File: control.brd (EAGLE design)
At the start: 186 x 186 mm, 103 parts, among them CN1 40PIN FPC, CN2 MINI B USB, CN3 2X10 HEADER, CN4 2X10 HEADER, SW1 TACT, SW10 TACT, SW11 TACT, SW12 TACT, SW13 TACT, SW14 TACT, SW15 TACT, SW16 TACT, SW2 TACT, SW3 TACT, SW4 TACT, SW5 TACT, SW6 TACT, SW7 TACT, SW8 TACT, SW9 TACT, U1 STM32H743ZI, U2 AS4C8M16SA, U3 TPS61169, U4 USBLC6-2SC6, U5 FT230X, U6 DCDC 3V3

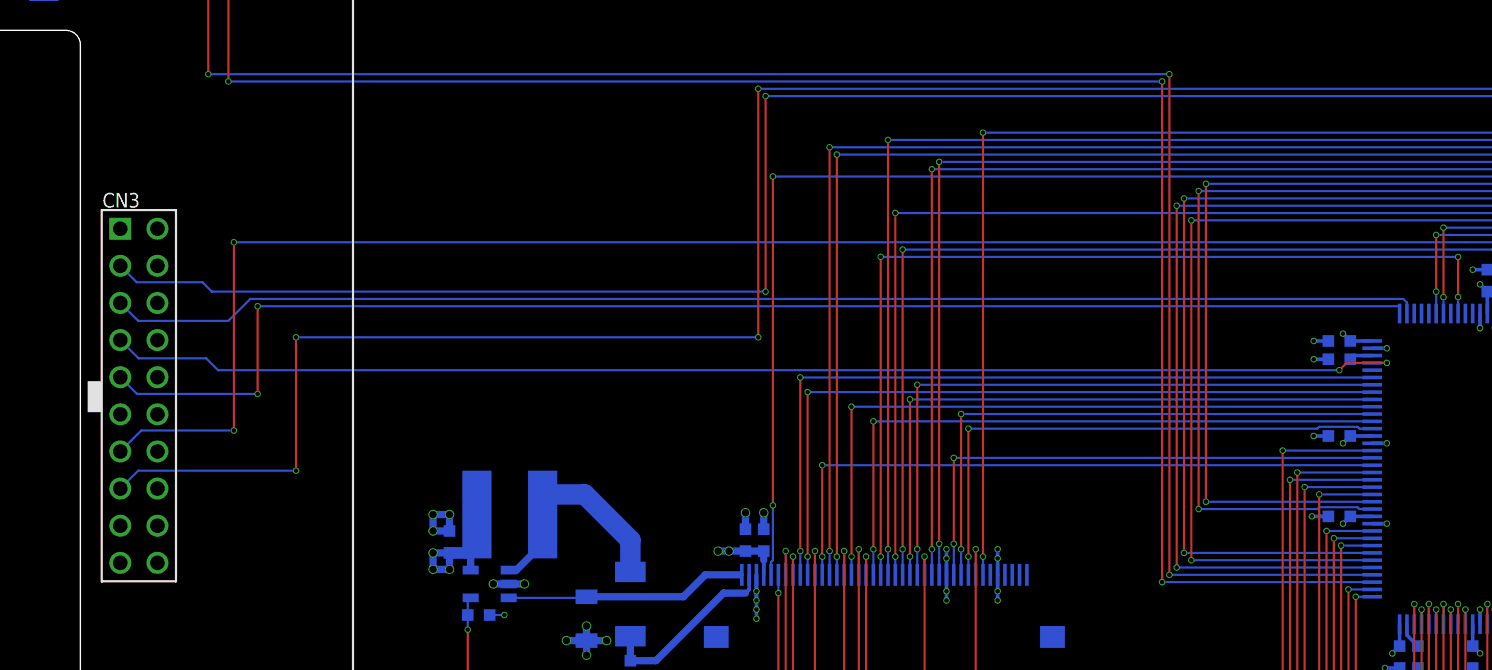
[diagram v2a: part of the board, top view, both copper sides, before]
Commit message: Corrected JTAG pinout
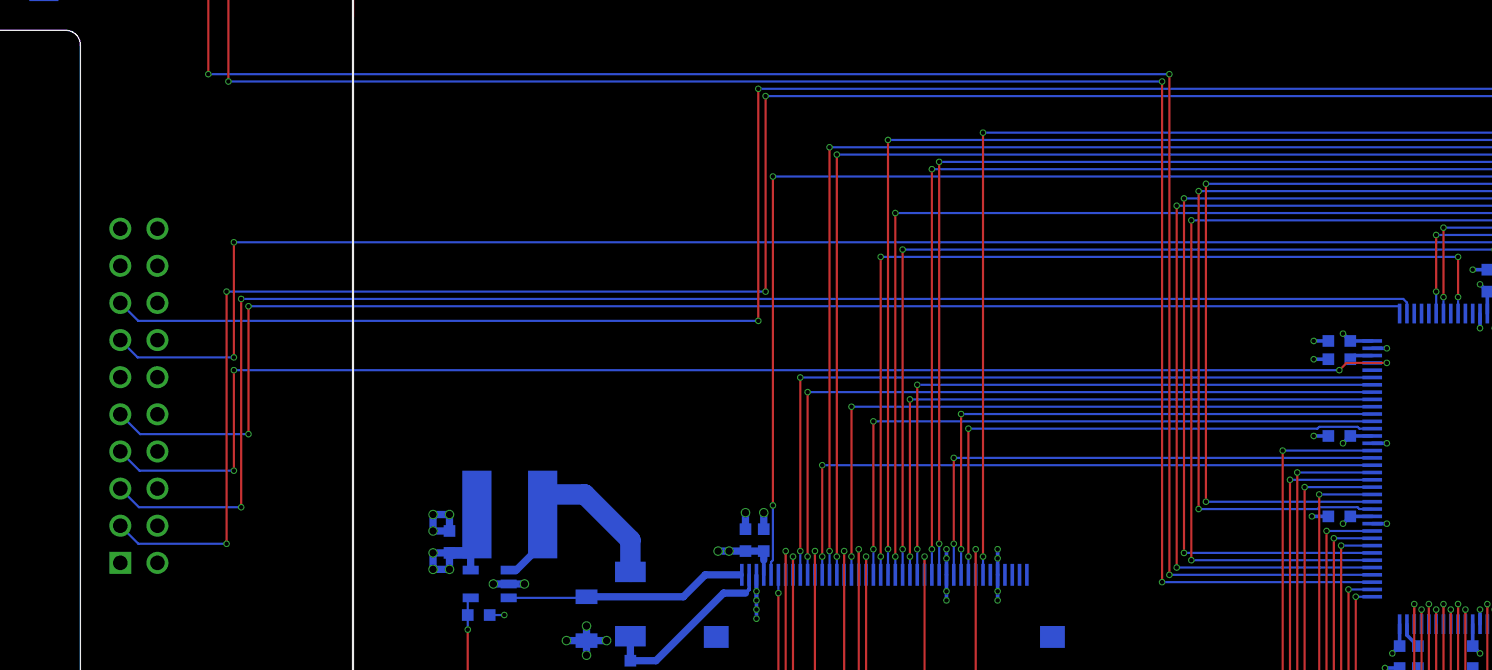
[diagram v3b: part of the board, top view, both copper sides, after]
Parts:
- flipped CN3 to the bottom, turned to 180 degrees
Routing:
- net JTAG_TRST: track 131.0 -> 148.0 mm, vias 4 -> 6
- net JTAG_TDI: track 90.0 -> 103.7 mm, vias 0 -> 2
- net STM_NRST: track 165.8 -> 155.5 mm, vias 6 -> 4
- net JTAG_TMS: track 88.7 -> 95.3 mm, vias 2 -> 4
- net JTAG_TDO: track 120.6 -> 115.5 mm
- net JTAG_TCK: track 94.5 -> 97.3 mm
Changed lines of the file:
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@@
 </layers>
 <board>
-<fusionsync huburn="a.cGVyc29uYWw6dWUyYjllNWFm" projecturn="a.cGVyc29uYWw6dWUyYjllNWFmIzIwMjAwODI1MzI2NDUzNDMx" f3durn="urn:adsk.wipprod:dm.lineage:wnPGf6KyQv68ik76HDulcw" pcbguid="" lastpulledtime="" lastsyncedchangeguid="" latestrevisionid="2ca1d1ef-4991-43c0-8b65-6e747995f1e9" lastsyncedrevisionid="2ca1d1ef-4991-43c0-8b65-6e747995f1e9" lastboardhashguid="514c7081-e8dd-fae7-9cc8-94f32975e53f" lastpushedtime="2020-10-09T13:18:08Z" linktopcb3d="true"/>
+<fusionsync huburn="a.cGVyc29uYWw6dWUyYjllNWFm" projecturn="a.cGVyc29uYWw6dWUyYjllNWFmIzIwMjAwODI1MzI2NDUzNDMx" f3durn="urn:adsk.wipprod:dm.lineage:wnPGf6KyQv68ik76HDulcw" pcbguid="" lastpulledtime="" lastsyncedchangeguid="" latestrevisionid="627856e7-1b0d-4a68-b278-4b2f0657c420" lastsyncedrevisionid="627856e7-1b0d-4a68-b278-4b2f0657c420" lastboardhashguid="c3fb2801-7401-a368-981a-5568be5e23b0" lastpushedtime="2020-10-11T09:29:11Z" linktopcb3d="true"/>
 <plain>
 <wire x1="90" y1="-93" x2="93" y2="-90" width="0" layer="20" curve="90" locked="yes"/>
@@
 <wire x1="60.35" y1="5" x2="55.35" y2="5" width="0.15" layer="29"/>
 <wire x1="60.35" y1="10" x2="60.35" y2="5" width="0.15" layer="29"/>
-<rectangle x1="-78.5" y1="48.875" x2="-77.5" y2="51" layer="21"/>
+<rectangle x1="-78.5" y1="48.875" x2="-77.5" y2="51" layer="22" rot="R180"/>
 </plain>
 <attributes>
@@
 </class>
 </classes>
-<designrules name="myDRC 4 layers 0.15mm">
+<designrules name="myDRC 4 layers 0.15mm *">
 <description language="de">&lt;b&gt;EAGLE Design Rules&lt;/b&gt;
 &lt;p&gt;
@@
 <param name="layerSetup" value="(1*2*3*16)"/>
 <param name="mtCopper" value="0.035mm 0.035mm 0.035mm 0.035mm 0.035mm 0.035mm 0.035mm 0.035mm 0.035mm 0.035mm 0.035mm 0.035mm 0.035mm 0.035mm 0.035mm 0.035mm"/>
-<param name="mtIsolate" value="1.5mm 0.15mm 0.2mm 0.15mm 0.2mm 0.15mm 0.2mm 0.15mm 0.2mm 0.15mm 0.2mm 0.15mm 0.2mm 0.15mm 0.2mm"/>
+<param name="mtIsolate" value="0.15mm 1.11mm 0.2mm 0.15mm 0.2mm 0.15mm 0.2mm 0.15mm 0.2mm 0.15mm 0.2mm 0.15mm 0.2mm 0.15mm 0.2mm"/>
 <param name="mdWireWire" value="0.15mm"/>
 <param name="mdWirePad" value="0.15mm"/>
@@
 <attribute name="PRICE_PER" value="0.2" x="31.75" y="-6" size="1.778" layer="27" rot="R90" display="off"/>
 </element>
-<element name="CN3" library="CONNECTORs" package="2X10PIN_HEADER" value="2X10 HEADER" x="-75" y="50" smashed="yes">
-<attribute name="DIGIKEY" value="2057-PH2-20-UA-ND" x="-75" y="50" size="1.778" layer="27" display="off"/>
-<attribute name="HEIGHT" value="10" x="-75" y="50" size="1.778" layer="27" display="off"/>
-<attribute name="NAME" x="-77.5" y="62.875" size="1" layer="25"/>
-<attribute name="PRICE_PER" value="0.2" x="-75" y="50" size="1.778" layer="27" display="off"/>
+<element name="CN3" library="CONNECTORs" package="2X10PIN_HEADER" value="2X10 HEADER" x="-75" y="50" smashed="yes" rot="MR180">
+<attribute name="DIGIKEY" value="2057-PH2-20-UA-ND" x="-75" y="50" size="1.778" layer="28" rot="MR180" display="off"/>
+<attribute name="HEIGHT" value="10" x="-75" y="50" size="1.778" layer="28" rot="MR180" display="off"/>
+<attribute name="NAME" x="-77.5" y="37.125" size="1" layer="26" rot="MR180"/>
+<attribute name="PRICE_PER" value="0.2" x="-75" y="50" size="1.778" layer="28" rot="MR180" display="off"/>
 </element>
 <element name="R21" library="r_0603" package="0603" value="10R" x="27" y="57.875" smashed="yes" rot="MR90">
@@
 <via x="32.125" y="71" extent="1-16" drill="0.3"/>
 <via x="-32.625" y="71" extent="1-16" drill="0.3"/>
-<wire x1="-32.625" y1="71" x2="-32.625" y2="54" width="0.15" layer="1"/>
-<via x="-32.625" y="54" extent="1-16" drill="0.3"/>
-<wire x1="-32.625" y1="54" x2="-64.25" y2="54" width="0.15" layer="16"/>
+<wire x1="-32.625" y1="71" x2="-32.625" y2="55.125" width="0.15" layer="1"/>
+<via x="-32.625" y="55.125" extent="1-16" drill="0.3"/>
 <wire x1="32.125" y1="71" x2="-32.625" y2="71" width="0.15" layer="16"/>
 <wire x1="30.625" y1="41.75" x2="32.125" y2="41.75" width="0.15" layer="16"/>
 <wire x1="32.125" y1="41.75" x2="32.125" y2="42.75" width="0.15" layer="16"/>
-<via x="-64.25" y="54" extent="1-16" drill="0.3"/>
-<wire x1="-64.25" y1="54" x2="-64.25" y2="44.875" width="0.15" layer="1"/>
-<via x="-64.25" y="44.875" extent="1-16" drill="0.3"/>
-<wire x1="-64.25" y1="44.875" x2="-75.045" y2="44.875" width="0.15" layer="16"/>
-<wire x1="-75.045" y1="44.875" x2="-76.27" y2="43.65" width="0.15" layer="16"/>
+<wire x1="-75.045" y1="55.125" x2="-76.27" y2="56.35" width="0.15" layer="16"/>
+<wire x1="-32.625" y1="55.125" x2="-75.045" y2="55.125" width="0.15" layer="16"/>
 </signal>
 <signal name="N$1">
@@
 <wire x1="7.625" y1="52.25" x2="7.125" y2="51.75" width="0.15" layer="1"/>
 <via x="7.125" y="51.75" extent="1-16" drill="0.3"/>
-<wire x1="-69.585" y1="51.75" x2="-70.395" y2="52.56" width="0.15" layer="16"/>
-<wire x1="-70.395" y1="52.56" x2="-75.02" y2="52.56" width="0.15" layer="16"/>
-<wire x1="-75.02" y1="52.56" x2="-76.27" y2="53.81" width="0.15" layer="16"/>
-<wire x1="7.125" y1="51.75" x2="-69.585" y2="51.75" width="0.15" layer="16"/>
+<wire x1="7.125" y1="51.75" x2="-68.5" y2="51.75" width="0.15" layer="16"/>
+<via x="-68.5" y="51.75" extent="1-16" drill="0.3"/>
+<wire x1="-68.5" y1="51.75" x2="-68.5" y2="44.875" width="0.15" layer="1"/>
+<via x="-68.5" y="44.875" extent="1-16" drill="0.3"/>
+<wire x1="-68.5" y1="44.875" x2="-74.955" y2="44.875" width="0.15" layer="16"/>
+<wire x1="-74.955" y1="44.875" x2="-76.27" y2="46.19" width="0.15" layer="16"/>
 </signal>
 <signal name="JTAG_TCK">
@@
 <contactref element="CN3" pad="5"/>
 <wire x1="11.25" y1="55.625" x2="11.25" y2="56.125" width="0.15" layer="16"/>
-<wire x1="11.25" y1="56.125" x2="-66.875" y2="56.125" width="0.15" layer="16"/>
-<via x="-66.875" y="56.125" extent="1-16" drill="0.3"/>
-<wire x1="-66.875" y1="56.125" x2="-66.875" y2="50.125" width="0.15" layer="1"/>
-<via x="-66.875" y="50.125" extent="1-16" drill="0.3"/>
-<wire x1="-66.875" y1="50.125" x2="-75.125" y2="50.125" width="0.15" layer="16"/>
-<wire x1="-75.125" y1="50.125" x2="-76.27" y2="51.27" width="0.15" layer="16"/>
+<wire x1="11.25" y1="56.125" x2="-67.5" y2="56.125" width="0.15" layer="16"/>
+<via x="-67.5" y="56.125" extent="1-16" drill="0.3"/>
+<wire x1="-67.5" y1="56.125" x2="-67.5" y2="47.375" width="0.15" layer="1"/>
+<via x="-67.5" y="47.375" extent="1-16" drill="0.3"/>
+<wire x1="-67.5" y1="47.375" x2="-74.915" y2="47.375" width="0.15" layer="16"/>
+<wire x1="-74.915" y1="47.375" x2="-76.27" y2="48.73" width="0.15" layer="16"/>
 </signal>
 <signal name="JTAG_TDI">
@@
 <wire x1="11.75" y1="55.625" x2="11.75" y2="56.375" width="0.15" layer="16"/>
 <wire x1="11.75" y1="56.375" x2="11.5" y2="56.625" width="0.15" layer="16"/>
-<wire x1="-75.045" y1="55.125" x2="-76.27" y2="56.35" width="0.15" layer="16"/>
-<wire x1="11.5" y1="56.625" x2="-67.375" y2="56.625" width="0.15" layer="16"/>
-<wire x1="-67.375" y1="56.625" x2="-68.875" y2="55.125" width="0.15" layer="16"/>
-<wire x1="-68.875" y1="55.125" x2="-75.045" y2="55.125" width="0.15" layer="16"/>
+<wire x1="11.5" y1="56.625" x2="-68" y2="56.625" width="0.15" layer="16"/>
+<via x="-68" y="56.625" extent="1-16" drill="0.3"/>
+<wire x1="-68" y1="56.625" x2="-68" y2="42.375" width="0.15" layer="1"/>
+<via x="-68" y="42.375" extent="1-16" drill="0.3"/>
+<wire x1="-74.995" y1="42.375" x2="-76.27" y2="43.65" width="0.15" layer="16"/>
+<wire x1="-68" y1="42.375" x2="-74.995" y2="42.375" width="0.15" layer="16"/>
 </signal>
 <signal name="JTAG_TDO">
@@
 <via x="23.25" y="60.5" extent="1-16" drill="0.3"/>
 <via x="-68.5" y="60.5" extent="1-16" drill="0.3"/>
-<wire x1="-68.5" y1="60.5" x2="-68.5" y2="47.625" width="0.15" layer="1"/>
-<via x="-68.5" y="47.625" extent="1-16" drill="0.3"/>
-<wire x1="-68.5" y1="47.625" x2="-74.835" y2="47.625" width="0.15" layer="16"/>
-<wire x1="-74.835" y1="47.625" x2="-76.27" y2="46.19" width="0.15" layer="16"/>
+<wire x1="-68.5" y1="60.5" x2="-68.5" y2="52.625" width="0.15" layer="1"/>
+<via x="-68.5" y="52.625" extent="1-16" drill="0.3"/>
 <wire x1="23.25" y1="60.5" x2="-68.5" y2="60.5" width="0.15" layer="16"/>
+<wire x1="-68.5" y1="52.625" x2="-75.085" y2="52.625" width="0.15" layer="16"/>
+<wire x1="-75.085" y1="52.625" x2="-76.27" y2="53.81" width="0.15" layer="16"/>
 </signal>
 <signal name="JTAG_TRST">
@@
 <wire x1="-32.125" y1="70.5" x2="-32.125" y2="57.125" width="0.15" layer="1"/>
 <via x="-32.125" y="57.125" extent="1-16" drill="0.3"/>
-<wire x1="-70.005" y1="57.125" x2="-70.645" y2="57.765" width="0.15" layer="16"/>
-<wire x1="-70.645" y1="57.765" x2="-75.145" y2="57.765" width="0.15" layer="16"/>
-<wire x1="-75.145" y1="57.765" x2="-76.27" y2="58.89" width="0.15" layer="16"/>
-<wire x1="-32.125" y1="57.125" x2="-70.005" y2="57.125" width="0.15" layer="16"/>
+<wire x1="-32.125" y1="57.125" x2="-69" y2="57.125" width="0.15" layer="16"/>
+<wire x1="-76.27" y1="41.11" x2="-75.035" y2="39.875" width="0.15" layer="16"/>
+<wire x1="-75.035" y1="39.875" x2="-69" y2="39.875" width="0.15" layer="16"/>
+<via x="-69" y="39.875" extent="1-16" drill="0.3"/>
+<wire x1="-69" y1="39.875" x2="-69" y2="57.125" width="0.15" layer="1"/>
+<via x="-69" y="57.125" extent="1-16" drill="0.3"/>
 </signal>
 <signal name="DAC_I2C_SCL">
